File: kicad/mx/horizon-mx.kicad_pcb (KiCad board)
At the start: 2 copper layers, 266 x 76 mm, 116 parts, among them SW1 SW_Push, SW10 SW_Push, SW11 SW_Push, SW12 SW_Push, SW13 SW_Push, SW14 SW_Push, SW15 SW_Push, SW16 SW_Push, SW17 SW_Push, SW18 SW_Push, SW19 SW_Push, SW2 SW_Push, SW20 SW_Push, SW21 SW_Push, SW22 SW_Push, SW23 SW_Push, SW24 SW_Push, SW25 SW_Push, SW26 SW_Push, SW27 SW_Push, SW28 SW_Push, SW29 SW_Push, SW3 SW_Push, SW30 SW_Push, SW31 SW_Push, SW32 SW_Push, SW33 SW_Push, SW34 SW_Push, SW35 SW_Push, SW36 SW_Push, SW37 SW_Push, SW38 SW_Push, SW39 SW_Push, SW4 SW_Push, SW40 SW_Push, SW41 SW_Push, SW42 SW_Push, SW43 SW_Push, SW44 SW_Push, SW45 SW_Push, SW46 SW_Push, SW47 SW_Push, SW48 SW_Push, SW49 SW_Push, SW5 SW_Push, SW50 SW_Push, SW51 SW_Push, SW52 SW_Push, SW6 SW_Push, SW7 SW_Push, SW8 SW_Push, SW9 SW_Push, U1 PRO-MICRO

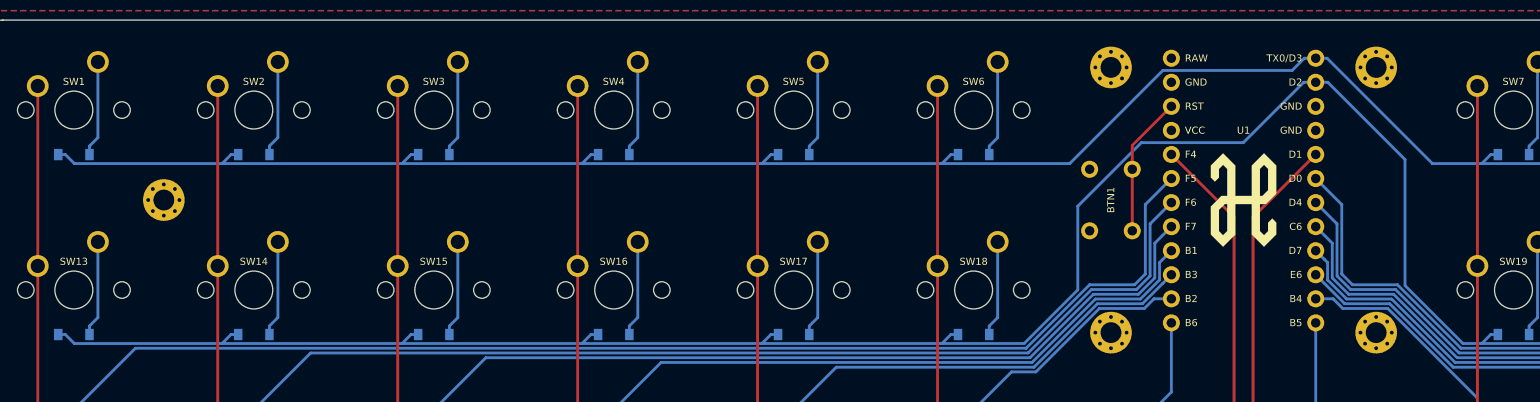
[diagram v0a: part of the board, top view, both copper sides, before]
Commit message: PCB revision 2.1, document revisions
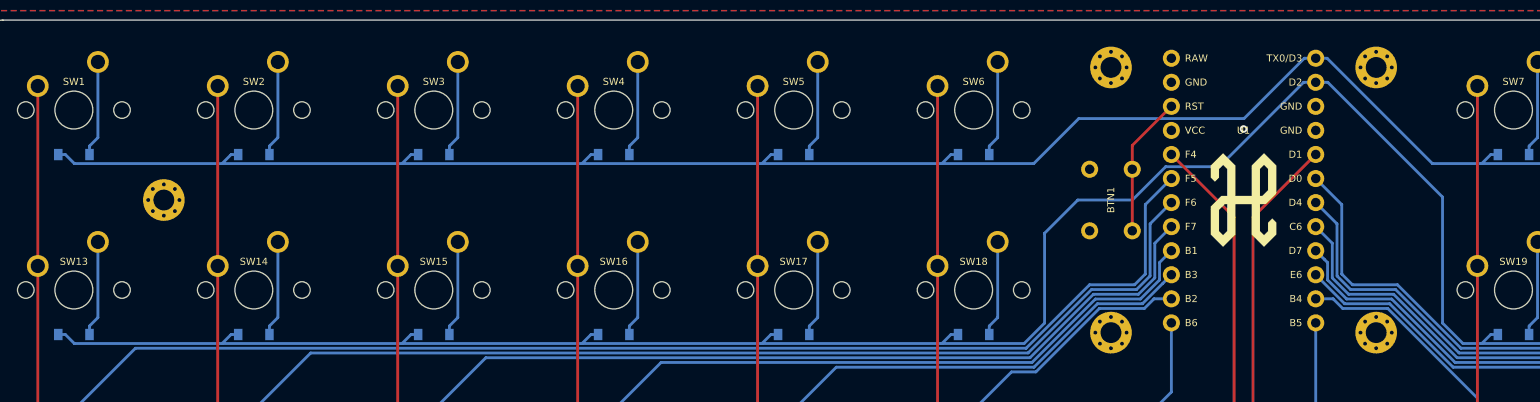
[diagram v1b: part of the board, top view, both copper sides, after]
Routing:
- net GND: vias 0 -> 1
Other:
- board text added: "rev2.1 | MX"
- board text removed: "rev2 | MX"
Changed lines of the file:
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@@
     (thickness 1.6)
     (drawings 27)
-    (tracks 394)
+    (tracks 397)
     (zones 0)
     (modules 116)
@@
   (title_block
     (title "Horizon MX")
-    (date 2021-10-13)
-    (rev 2)
+    (date 2021-10-24)
+    (rev 2.1)
     (company skarrmann)
   )
@@
     (effects (font (size 1 1) (thickness 0.15)) (justify mirror))
   )
-  (gr_text "rev2 | MX" (at 148 89.5) (layer B.SilkS)
+  (gr_text "rev2.1 | MX" (at 148 89.5) (layer B.SilkS)
     (effects (font (size 1 1) (thickness 0.15)) (justify mirror))
   )
@@
   (segment (start 156.82 71.03) (end 167.940001 82.150001) (width 0.3) (layer B.Cu) (net 2))
   (segment (start 155.62 71.03) (end 156.82 71.03) (width 0.3) (layer B.Cu) (net 2))
-  (segment (start 22.85 81.2) (end 23.6 81.2) (width 0.3) (layer B.Cu) (net 2))
   (segment (start 154.42 71.03) (end 155.62 71.03) (width 0.3) (layer B.Cu) (net 2))
   (segment (start 23.6 81.2) (end 24.550001 82.150001) (width 0.3) (layer B.Cu) (net 2))
-  (segment (start 24.550001 82.150001) (end 129.647997 82.150001) (width 0.3) (layer B.Cu) (net 2))
-  (segment (start 129.647997 82.150001) (end 139.477999 72.319999) (width 0.3) (layer B.Cu) (net 2))
-  (segment (start 139.477999 72.319999) (end 153.130001 72.319999) (width 0.3) (layer B.Cu) (net 2))
-  (segment (start 153.130001 72.319999) (end 154.42 71.03) (width 0.3) (layer B.Cu) (net 2))
+  (segment (start 22.85 81.2) (end 23.6 81.2) (width 0.3) (layer B.Cu) (net 2))
+  (segment (start 24.550001 82.150001) (end 125.849999 82.150001) (width 0.3) (layer B.Cu) (net 2))
+  (segment (start 125.849999 82.150001) (end 130.600001 77.399999) (width 0.3) (layer B.Cu) (net 2))
+  (segment (start 130.600001 77.399999) (end 148.050001 77.399999) (width 0.3) (layer B.Cu) (net 2))
+  (segment (start 148.050001 77.399999) (end 154.42 71.03) (width 0.3) (layer B.Cu) (net 2))
   (segment (start 45.15 80.3) (end 45.15 81.2) (width 0.3) (layer B.Cu) (net 3))
   (segment (start 46.04 79.41) (end 45.15 80.3) (width 0.3) (layer B.Cu) (net 3))
@@
   (segment (start 98.85 100.2) (end 98.1 100.2) (width 0.3) (layer B.Cu) (net 9))
   (segment (start 173.149999 101.150001) (end 268.149999 101.150001) (width 0.3) (layer B.Cu) (net 9))
-  (segment (start 23.6 100.2) (end 22.85 100.2) (width 0.3) (layer B.Cu) (net 9))
-  (segment (start 124.833277 101.150001) (end 24.550001 101.150001) (width 0.3) (layer B.Cu) (net 9))
-  (segment (start 155.62 73.57) (end 154.347208 73.57) (width 0.3) (layer B.Cu) (net 9))
-  (segment (start 24.550001 101.150001) (end 23.6 100.2) (width 0.3) (layer B.Cu) (net 9))
-  (segment (start 154.347208 73.57) (end 147.977209 79.939999) (width 0.3) (layer B.Cu) (net 9))
-  (segment (start 147.977209 79.939999) (end 137.209999 79.939999) (width 0.3) (layer B.Cu) (net 9))
-  (segment (start 137.209999 79.939999) (end 130.499999 86.649999) (width 0.3) (layer B.Cu) (net 9))
-  (segment (start 130.499999 86.649999) (end 130.499999 95.483279) (width 0.3) (layer B.Cu) (net 9))
-  (segment (start 130.499999 95.483279) (end 124.833277 101.150001) (width 0.3) (layer B.Cu) (net 9))
-  (segment (start 171.166723 101.150001) (end 173.149999 101.150001) (width 0.3) (layer B.Cu) (net 9))
-  (segment (start 165.050001 95.033279) (end 171.166723 101.150001) (width 0.3) (layer B.Cu) (net 9))
-  (segment (start 165.050001 81.727209) (end 165.050001 95.033279) (width 0.3) (layer B.Cu) (net 9))
-  (segment (start 156.892792 73.57) (end 165.050001 81.727209) (width 0.3) (layer B.Cu) (net 9))
-  (segment (start 155.62 73.57) (end 156.892792 73.57) (width 0.3) (layer B.Cu) (net 9))
+  (segment (start 154.347208 73.57) (end 155.62 73.57) (width 0.3) (layer B.Cu) (net 9))
+  (segment (start 139.779999 82.479999) (end 145.437209 82.479999) (width 0.3) (layer B.Cu) (net 9))
+  (segment (start 136.259998 86) (end 139.779999 82.479999) (width 0.3) (layer B.Cu) (net 9))
+  (segment (start 130.5 86) (end 136.259998 86) (width 0.3) (layer B.Cu) (net 9))
+  (segment (start 145.437209 82.479999) (end 154.347208 73.57) (width 0.3) (layer B.Cu) (net 9))
+  (segment (start 23.6 100.2) (end 24.550001 101.150001) (width 0.3) (layer B.Cu) (net 9))
+  (segment (start 24.550001 101.150001) (end 124.833277 101.150001) (width 0.3) (layer B.Cu) (net 9))
+  (segment (start 22.85 100.2) (end 23.6 100.2) (width 0.3) (layer B.Cu) (net 9))
+  (segment (start 124.833277 101.150001) (end 126.991639 98.991639) (width 0.3) (layer B.Cu) (net 9))
+  (segment (start 126.991639 98.991639) (end 126.991639 89.508361) (width 0.3) (layer B.Cu) (net 9))
+  (segment (start 126.991639 89.508361) (end 130.5 86) (width 0.3) (layer B.Cu) (net 9))
+  (segment (start 156.892792 73.57) (end 155.62 73.57) (width 0.3) (layer B.Cu) (net 9))
+  (segment (start 169.008361 85.685569) (end 156.892792 73.57) (width 0.3) (layer B.Cu) (net 9))
+  (segment (start 169.008361 98.991639) (end 169.008361 85.685569) (width 0.3) (layer B.Cu) (net 9))
+  (segment (start 171.166723 101.150001) (end 169.008361 98.991639) (width 0.3) (layer B.Cu) (net 9))
+  (segment (start 173.149999 101.150001) (end 171.166723 101.150001) (width 0.3) (layer B.Cu) (net 9))
   (segment (start 198.04 71.42) (end 198.04 79.41) (width 0.3) (layer B.Cu) (net 10))
   (segment (start 197.15 80.3) (end 197.15 81.2) (width 0.3) (layer B.Cu) (net 10))
@@
   (segment (start 23.6 119.2) (end 24.550001 120.150001) (width 0.3) (layer B.Cu) (net 16))
   (segment (start 155.62 81.19) (end 149 87.81) (width 0.3) (layer F.Cu) (net 16))
-  (via (at 149.849999 120.150001) (size 0.8) (drill 0.4) (layers F.Cu B.Cu) (net 16) (status 1000000))
+  (via (at 149.849999 120.150001) (size 0.8) (drill 0.4) (layers F.Cu B.Cu) (net 16))
   (segment (start 149 119.300002) (end 149.849999 120.150001) (width 0.3) (layer F.Cu) (net 16))
   (segment (start 149 87.81) (end 149 119.300002) (width 0.3) (layer F.Cu) (net 16))
@@
   (segment (start 83.15 137.3) (end 83.15 138.2) (width 0.3) (layer B.Cu) (net 46))
   (segment (start 84.04 128.42) (end 84.04 136.41) (width 0.3) (layer B.Cu) (net 46))
+  (via (at 148 78.5) (size 0.8) (drill 0.4) (layers F.Cu B.Cu) (net 47))
   (segment (start 20.69 73.96) (end 20.69 130.96) (width 0.3) (layer F.Cu) (net 48))
   (segment (start 30.999989 101.650011) (end 20.69 111.96) (width 0.3) (layer B.Cu) (net 48))
